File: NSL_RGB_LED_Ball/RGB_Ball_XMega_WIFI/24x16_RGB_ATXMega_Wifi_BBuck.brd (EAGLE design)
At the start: 46.4 x 123.7 mm, 118 parts, among them IC2 TLC5947XLP, IC3 TLC5947XLP, IC4 TLC5947XLP, IC5 MCP73123, IC6 CC3000, IC7 MMA7455L, IC8 OPA344, U1 TPS6120x, X1 NX3225GA-16.000M-STD-CRG-2

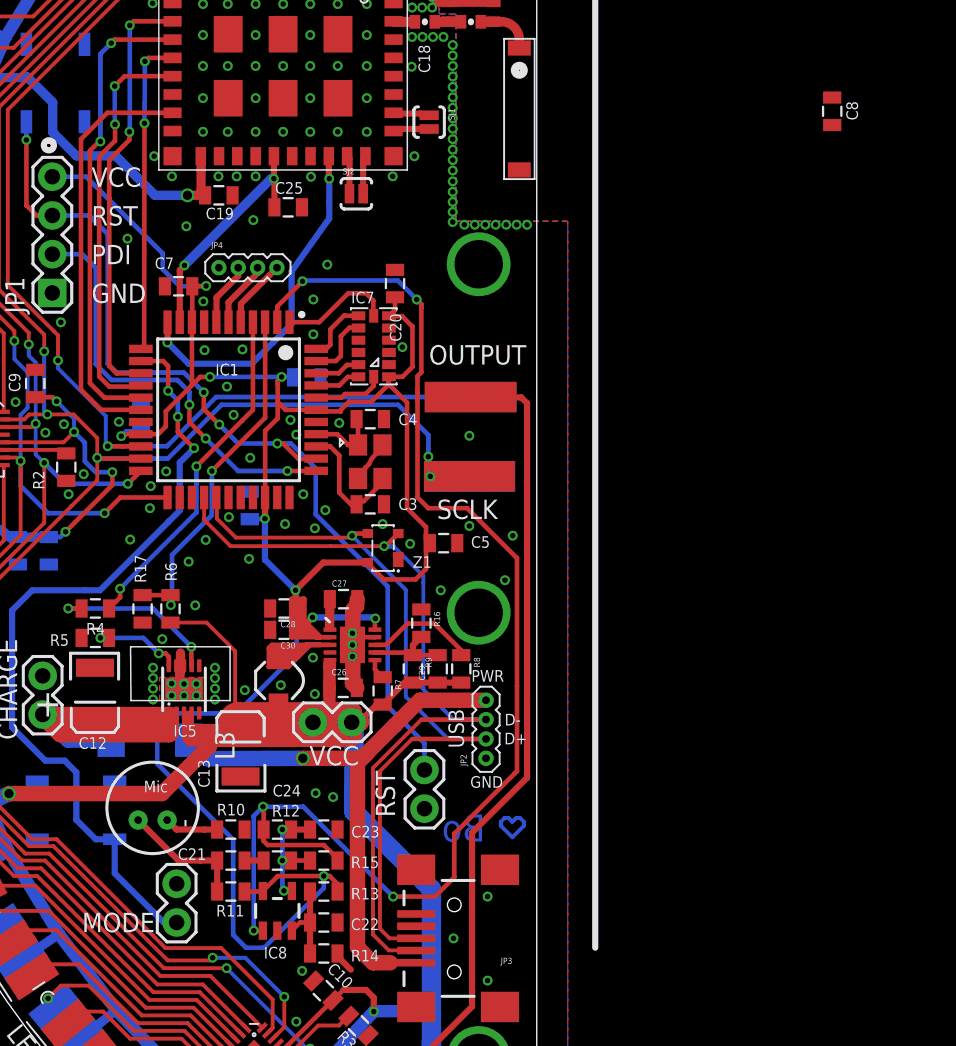
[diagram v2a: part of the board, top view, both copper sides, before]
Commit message: 
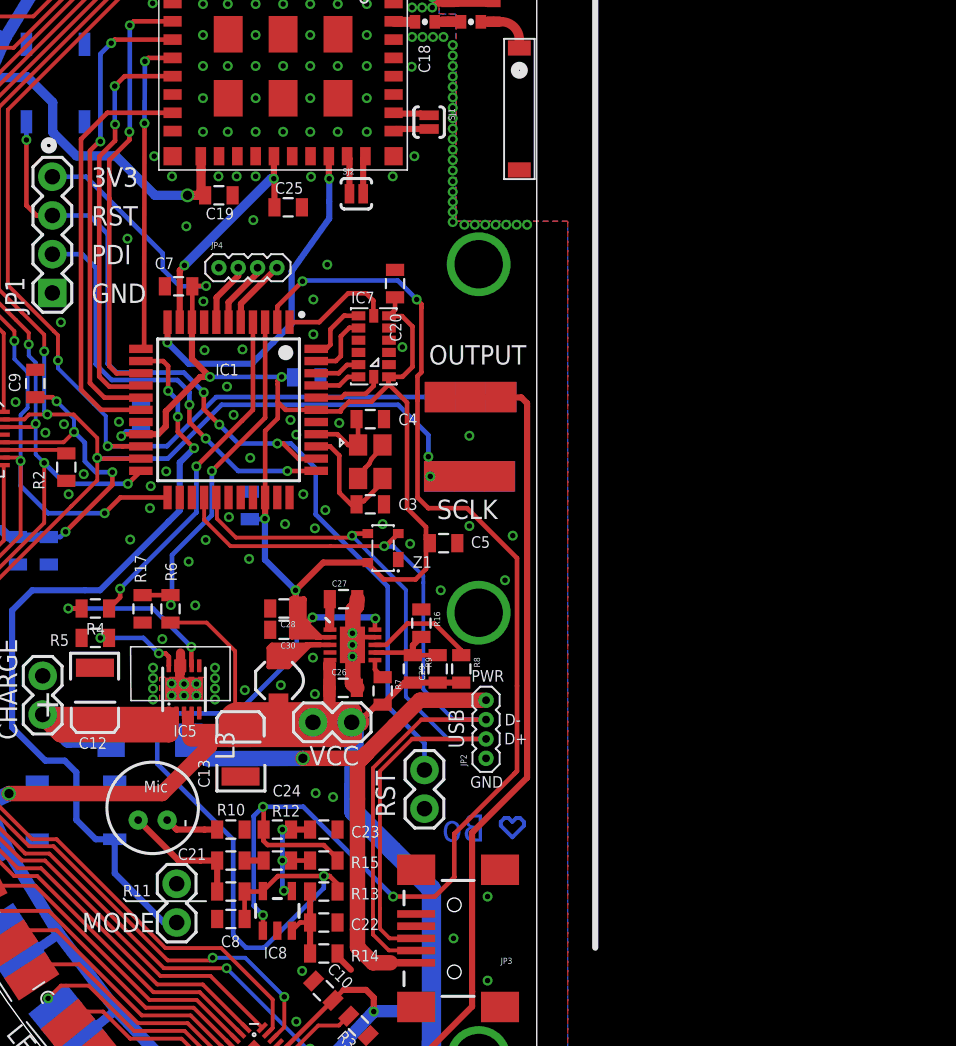
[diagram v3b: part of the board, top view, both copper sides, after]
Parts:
- moved C8 66.1 mm to (-37.8, -31.5), turned to 180 degrees
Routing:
- net +3V3: track 162.3 -> 164.1 mm
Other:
- board text added: "3V3"
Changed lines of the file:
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@@
 <text x="-46.99" y="11.43" size="1.27" layer="21" font="vector" ratio="12">PDI</text>
 <text x="-46.99" y="13.97" size="1.27" layer="21" font="vector" ratio="12">RST</text>
-<text x="-46.99" y="16.51" size="1.27" layer="21" font="vector" ratio="12">VCC</text>
+<text x="-46.99" y="16.51" size="1.27" layer="21" font="vector" ratio="12">3V3</text>
 <text x="-46.99" y="8.89" size="1.27" layer="21" font="vector" ratio="12">GND</text>
 <circle x="-49.784" y="19.2278" radius="0.331175" width="0.4064" layer="21"/>
@@
 <text x="-22.5806" y="-25.5524" size="1.778" layer="16" font="vector" ratio="12" rot="MR180" align="center">Bo</text>
 <wire x1="-13.9192" y1="32.3088" x2="11.6078" y2="32.3088" width="0" layer="21"/>
+<wire x1="-44.8818" y1="-30.1752" x2="-44.704" y2="-30.353" width="0.127" layer="21"/>
+<wire x1="-44.704" y1="-30.353" x2="-39.4716" y2="-30.353" width="0.127" layer="21"/>
 </plain>
 <attributes>
@@
 </element>
 <element name="R11" library="SparkFun" package="0805" value="2.2k" x="-37.846" y="-29.718" smashed="yes">
-<attribute name="NAME" x="-38.8112" y="-31.3563" size="0.762" layer="21" font="vector" ratio="12"/>
+<attribute name="NAME" x="-44.9326" y="-30.0355" size="0.762" layer="21" font="vector" ratio="12"/>
 <attribute name="VALUE" x="-38.862" y="-31.115" size="0.4064" layer="27"/>
 <attribute name="OC_NEWARK" value="61M5457" x="-37.846" y="-29.718" size="1.778" layer="27" display="off"/>
@@
 <attribute name="VALUE" x="-37.9984" y="1.8796" size="0.7" layer="21" ratio="5" rot="R270"/>
 </element>
-<element name="C8" library="SparkFun" package="0805" value="0.1uF" x="1.6002" y="21.463" smashed="yes" rot="R270">
-<attribute name="NAME" x="2.5273" y="22.1234" size="0.762" layer="21" font="vector" rot="R270"/>
-<attribute name="VALUE" x="0.2032" y="22.479" size="0.4064" layer="27" rot="R270"/>
+<element name="C8" library="SparkFun" package="0805" value="0.1uF" x="-37.846" y="-31.5214" smashed="yes" rot="R180">
+<attribute name="NAME" x="-37.2364" y="-32.6009" size="0.762" layer="21" font="vector" ratio="12" rot="R180"/>
+<attribute name="VALUE" x="-36.83" y="-30.1244" size="0.4064" layer="27" rot="R180"/>
 </element>
 <element name="X1" library="24x16_RGB_ATXMega_Wifi" package="NX3225GA" value="NX3225GA-16.000M-STD-CRG-2" x="-28.702" y="-1.524" smashed="yes" rot="R270"/>
@@
 <wire x1="-35.698" y1="-25.654" x2="-35.698" y2="-24.1952" width="0.3048" layer="1"/>
 <wire x1="-35.698" y1="-24.1952" x2="-35.7378" y2="-24.1554" width="0.3048" layer="1"/>
-<wire x1="-35.748" y1="-32.2881" x2="-36.3427" y2="-32.2881" width="0.3048" layer="1"/>
-<wire x1="-36.3427" y1="-32.2881" x2="-36.3474" y2="-32.2834" width="0.3048" layer="1"/>
-<via x="-36.3474" y="-32.2834" extent="1-16" drill="0.3556"/>
-<wire x1="-36.3474" y1="-32.2834" x2="-36.3474" y2="-24.765" width="0.3048" layer="16"/>
+<wire x1="-35.748" y1="-32.2881" x2="-35.7331" y2="-32.2881" width="0.3048" layer="1"/>
+<wire x1="-35.7331" y1="-32.2881" x2="-35.7378" y2="-31.2674" width="0.3048" layer="1"/>
+<via x="-35.7378" y="-31.2674" extent="1-16" drill="0.3556"/>
 <wire x1="-36.3474" y1="-24.765" x2="-35.7378" y2="-24.1554" width="0.3048" layer="16"/>
 <wire x1="-30.85" y1="-27.686" x2="-30.85" y2="-27.57" width="0.3048" layer="1"/>
@@
 <wire x1="-25.6032" y1="-3.8608" x2="-24.892" y2="-4.572" width="0.3048" layer="1"/>
 <wire x1="-24.892" y1="-4.572" x2="-22.352" y2="-4.572" width="0.3048" layer="1"/>
+<wire x1="-36.3474" y1="-24.765" x2="-36.3474" y2="-30.6578" width="0.3048" layer="16"/>
+<wire x1="-36.3474" y1="-30.6578" x2="-35.7378" y2="-31.2674" width="0.3048" layer="16"/>
 </signal>
 <signal name="CHARGE">
@@
 <via x="-32.3342" y="-16.764" extent="1-16" drill="0.3556"/>
 <via x="-34.5694" y="-16.1798" extent="1-16" drill="0.3556"/>
-<wire x1="-18.415" y1="14.0208" x2="1.6002" y2="20.563" width="0" layer="19" extent="1-1"/>
 </signal>
 <signal name="N$7">
@@
 <wire x1="-28.8638" y1="-8.1382" x2="-28.9306" y2="-8.205" width="0.3048" layer="1"/>
 <wire x1="-43.7484" y1="0.2796" x2="-43.7482" y2="0.2794" width="0.3048" layer="1"/>
-<wire x1="-43.7482" y1="0.2794" x2="-42.6212" y2="0.2794" width="0.3048" layer="1"/>
-<wire x1="-42.6212" y1="0.2794" x2="-42.1132" y2="0.7874" width="0.3048" layer="1"/>
-<wire x1="-42.1132" y1="0.7874" x2="-42.1132" y2="1.778" width="0.3048" layer="1"/>
-<wire x1="-42.1132" y1="1.778" x2="-40.3984" y2="3.4928" width="0.3048" layer="1"/>
-<wire x1="-40.3984" y1="3.4928" x2="-40.3984" y2="7.6296" width="0.3048" layer="1"/>
 <wire x1="-35.5984" y1="-3.8704" x2="-35.5984" y2="0.495" width="0.3048" layer="1"/>
-<wire x1="-40.3984" y1="3.4928" x2="-39.8526" y2="4.0386" width="0.3048" layer="1"/>
 <wire x1="-40.3984" y1="7.6296" x2="-40.375" y2="7.653" width="0.3048" layer="1"/>
 <wire x1="-40.375" y1="7.653" x2="-40.375" y2="9.9822" width="0.3048" layer="1"/>
@@
 <wire x1="-27.0764" y1="9.26" x2="-27.0764" y2="8.4422" width="0.3048" layer="1"/>
 <wire x1="-27.0764" y1="8.4422" x2="-27.4734" y2="8.0452" width="0.3048" layer="1"/>
-<wire x1="-39.8526" y1="4.0386" x2="-39.2176" y2="4.0386" width="0.3048" layer="1"/>
 <via x="-39.2176" y="4.0386" extent="1-16" drill="0.3556"/>
 <wire x1="-39.2176" y1="4.0386" x2="-34.5186" y2="4.0386" width="0.3048" layer="16"/>
@@
 <wire x1="-24.791421875" y1="-6.867346875" x2="-25.0444" y2="-6.61436875" width="0.3048" layer="1"/>
 <wire x1="-25.0444" y1="-6.61436875" x2="-25.0444" y2="-6.3246" width="0.3048" layer="1"/>
-<wire x1="-25.9334" y1="7.3406" x2="1.6002" y2="22.363" width="0" layer="19" extent="1-1"/>
+<wire x1="-40.3984" y1="7.6296" x2="-40.3984" y2="5.2194" width="0.4064" layer="1"/>
+<wire x1="-40.3984" y1="5.2194" x2="-39.2176" y2="4.0386" width="0.4064" layer="1"/>
+<wire x1="-43.7482" y1="0.2794" x2="-42.6212" y2="0.2794" width="0.4064" layer="1"/>
+<wire x1="-42.6212" y1="0.2794" x2="-42.1132" y2="0.7874" width="0.4064" layer="1"/>
+<wire x1="-42.1132" y1="0.7874" x2="-42.1132" y2="1.778" width="0.4064" layer="1"/>
+<wire x1="-42.1132" y1="1.778" x2="-39.8526" y2="4.0386" width="0.4064" layer="1"/>
+<wire x1="-39.8526" y1="4.0386" x2="-39.2176" y2="4.0386" width="0.4064" layer="1"/>
+<wire x1="-36.946" y1="-31.5214" x2="-36.946" y2="-29.718" width="0.3048" layer="1"/>
 </signal>
 <signal name="N$24">

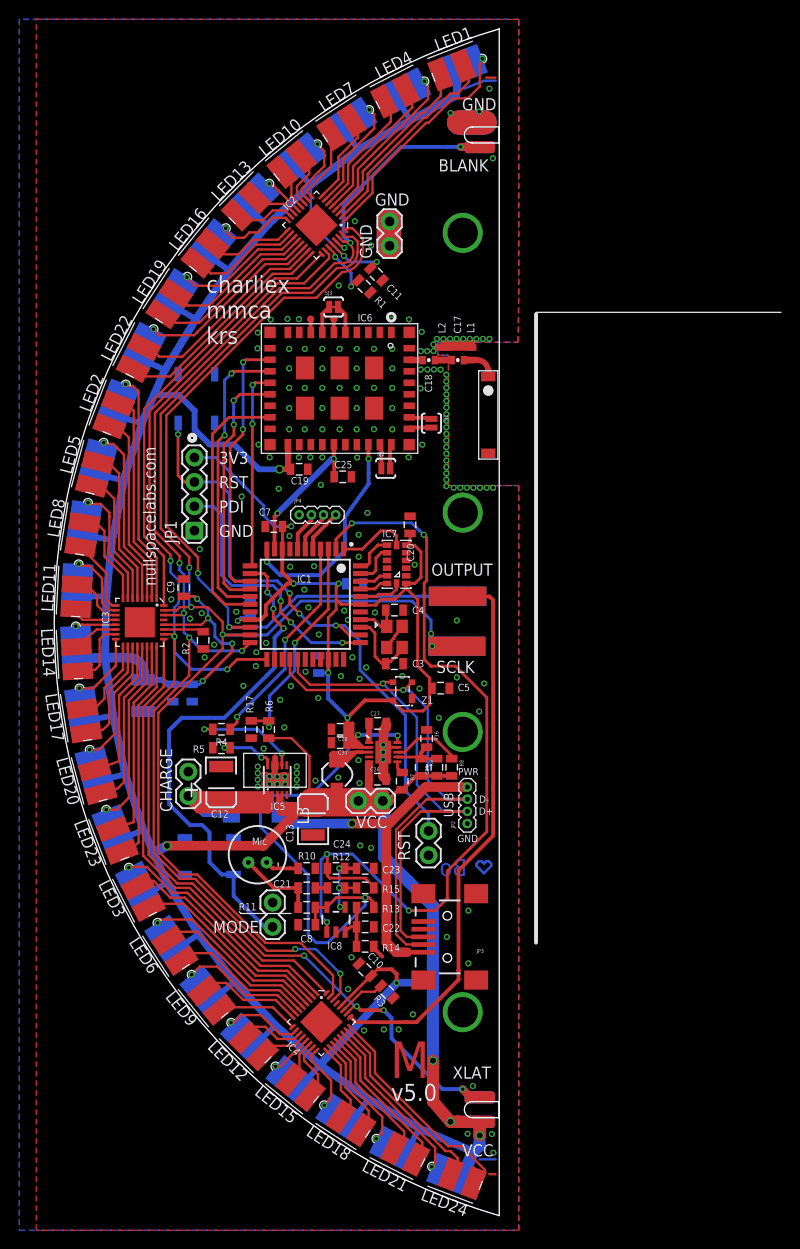
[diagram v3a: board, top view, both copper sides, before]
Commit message: 
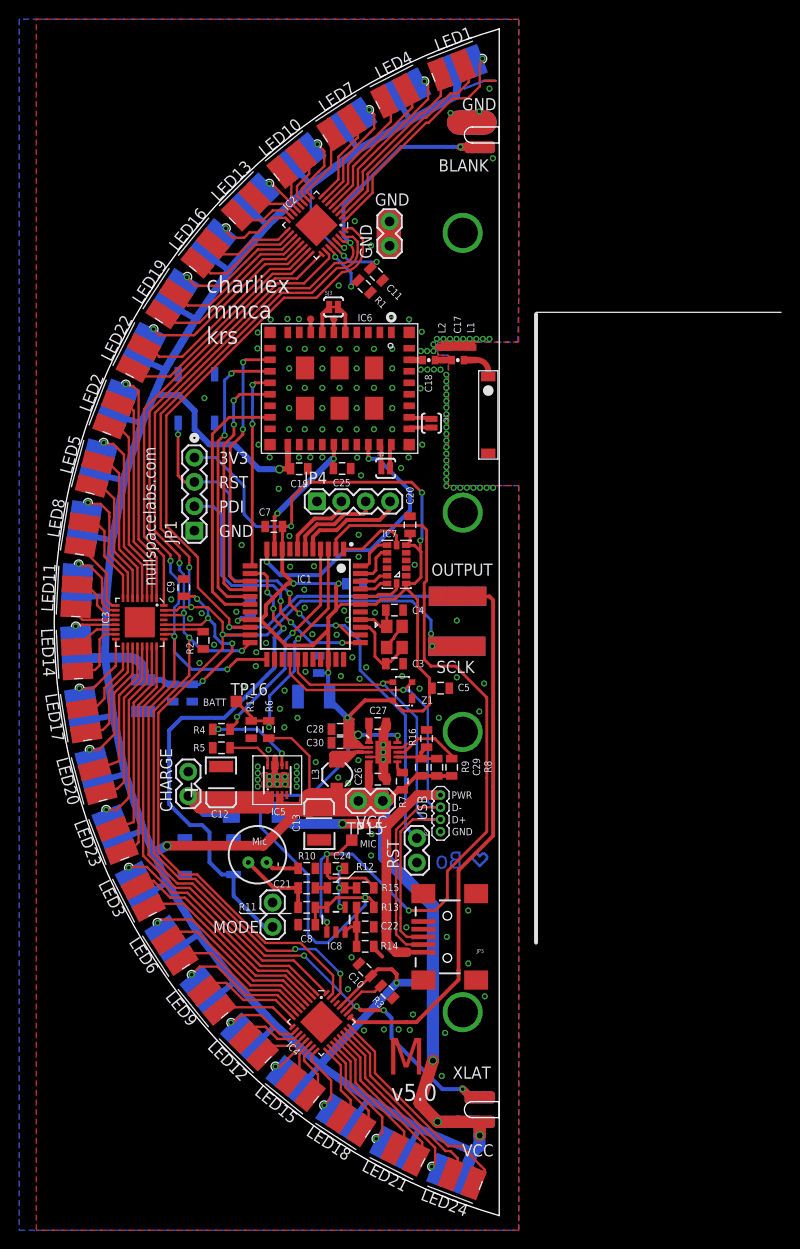
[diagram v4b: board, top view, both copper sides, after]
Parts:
- added C31: 12pF, SparkFun:0805
- added C32: 1uF, 24x16_RGB:0805
- added TP15: MIC, testpad:TP12SQ
- added TP16: BATT, testpad:TP12SQ
- C23: value .1uF -> 47uF; device SparkFun:0805 -> slice_noshift:EIA3528
- JP4: device SparkFun-Connectors:1X04-1.27MM -> SparkFun-Connectors:1X04
- R1, R2, R3: value 47K -> 20K
- moved C23 18.7 mm to (-37.1, -7.75), flipped to the bottom, turned to 180 degrees
- moved JP2 2.92 mm to (-23.9, -21.8)
- moved JP4 2.32 mm to (-36.8, 12.6)
- moved RST 1.44 mm to (-26.4, -25.0)
- moved C25 0.87 mm to (-34.2, 16.0)
- moved C13 0.83 mm to (-36.6, -21.0)
- moved C19 0.05 mm to (-38.6, 16.0)
- moved C26 0.05 mm to (-30.4, -16.4)
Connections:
- net +3V3: now also C23.A, C31.1, C32.1
- net BATTSENSE: now also TP16.TP
- net GND: now also C23.C, C31.2, C32.2; no longer C23.2
- net MIC: now also TP15.TP
- net N$17: no longer C23.1
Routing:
- net +3V3: track 164.1 -> 203.7 mm, vias 9 -> 11
- net UP: track 4.56 -> 11.3 mm
- net VCC: track 453.5 -> 459.9 mm
- net VBAT_SW_EN: track 23.2 -> 28.9 mm
- net GND: track 38.7 -> 44.2 mm, vias 177 -> 179
- net SELECT: track 4.36 -> 9.78 mm
- net D-: track 53.9 -> 49.7 mm
- net D+: track 51.2 -> 47.3 mm
- net DOWN: track 4.17 -> 7.90 mm
- net MIC: track 87.9 -> 91.3 mm, vias 5 -> 3
- net N$7: track 38.8 -> 35.7 mm
- net BATTSENSE: track 23.6 -> 26.3 mm
- net N$1: track 11.3 -> 9.54 mm
- net N$34: track 1.68 -> 0.00 mm
- net N$17: track 8.22 -> 6.97 mm
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
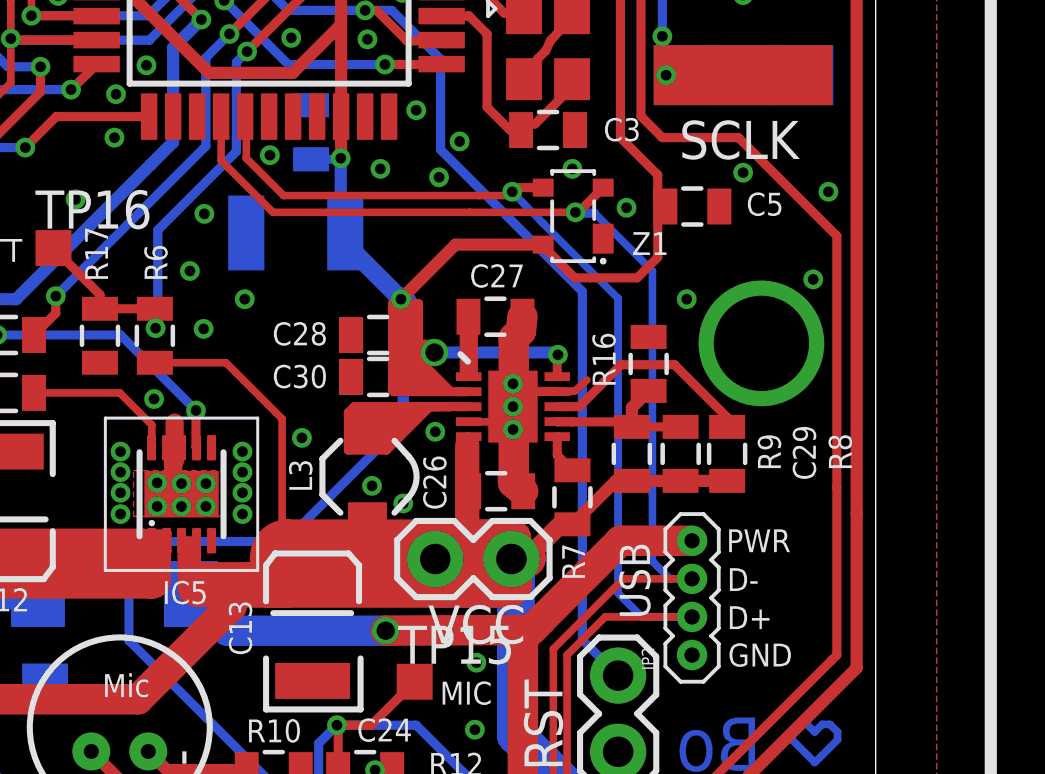
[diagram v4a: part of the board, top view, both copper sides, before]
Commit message: Changed to Buck Boost
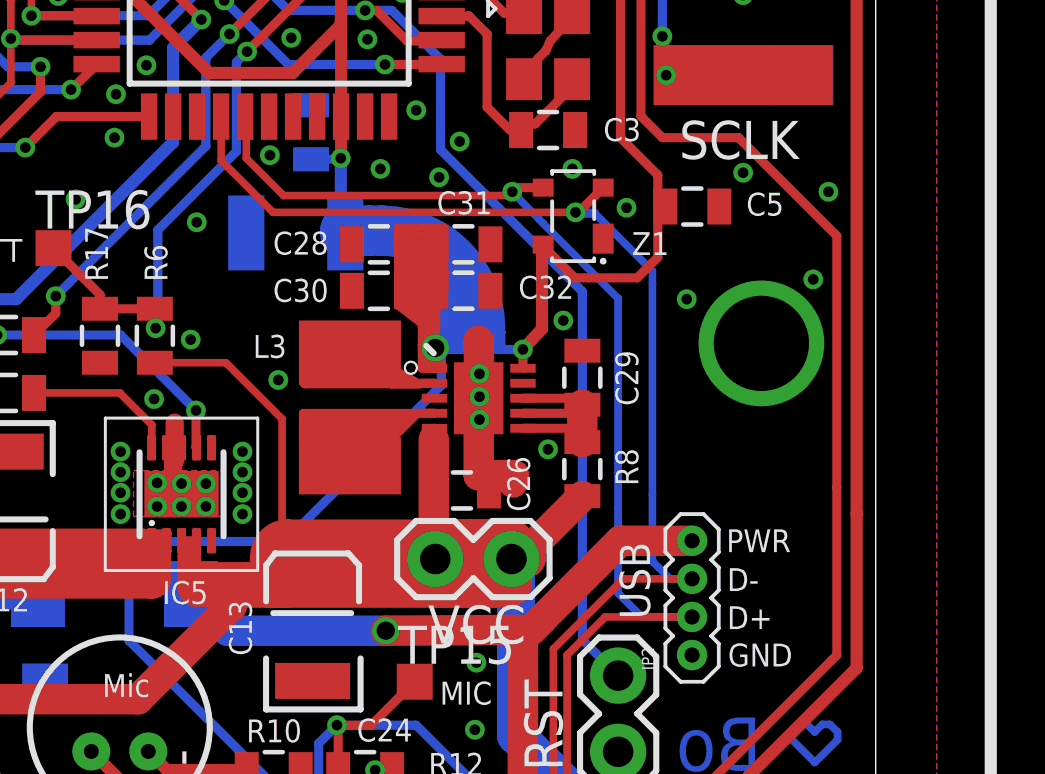
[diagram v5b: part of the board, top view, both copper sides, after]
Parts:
- removed C27: 0.1, CH_passive:0805
- removed R16, R9: see notes, CH_passive:0805
- removed R7: 1M, CH_passive:0805
- removed U1: TPS6120x, CH_TI:QFN_10_PAD
- added IC9: TPS6300X, 24x16_RGB_ATXMega_Wifi_BBuck:QFN_10_PAD
- L3: value 2.2uH 1.6A -> (none); device CH_passive:1_3X1_3 -> rcl:L1812
- R8: value 1M -> 100R
- moved C31 5.26 mm to (-31.5, -8.13), flipped to the top
- moved R8 4.85 mm to (-27.6, -15.6)
- moved C29 4.15 mm to (-27.6, -12.6), turned to 270 degrees
- moved C32 3.20 mm to (-31.5, -9.68), flipped to the top
- moved C28 3.02 mm to (-34.3, -8.13)
- moved C30 2.87 mm to (-34.3, -9.68)
- moved L3 2.38 mm to (-35.3, -13.6)
- moved C26 1.14 mm to (-31.6, -16.3)
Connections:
- removed net EN: R7.1, U1.6
- removed net PS: R8.1, U1.8
- removed net UVLO: C29.2, R16.2, R9.1, U1.7
- new net N$32: C29.2, IC9.6, IC9.7, IC9.8, R8.1
- net +3V3: now also IC9.1, IC9.10; no longer U1.10, U1.2
- net GND: now also C29.1, IC9.3, IC9.9, IC9.PAD@1, IC9.PAD@2, IC9.PAD@3, IC9.PAD@4, IC9.PAD@5; no longer C27.2, R16.1, U1.4, U1.9, U1.PAD@1, U1.PAD@2, U1.PAD@3, U1.PAD@4, U1.PAD@5
- net N$24: now also IC9.2, L3.2; no longer L3.P$2, U1.3
- net N$30: now also IC9.4, L3.1; no longer C27.1, U1.1
- net VCC: now also IC9.5; no longer C29.1, L3.P$1, R7.2, R9.2, U1.5
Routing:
- net +3V3: track 203.7 -> 225.7 mm, vias 11 -> 10
- net N$30: track 2.79 -> 24.6 mm
- net GND: track 44.2 -> 36.0 mm, vias 179 -> 176
- net N$32: track 0.00 -> 7.58 mm
- net PS: track 7.49 -> 0.00 mm
- net UVLO: track 6.36 -> 0.00 mm
- net VCC: track 459.9 -> 454.3 mm
- net N$24: track 16.9 -> 18.7 mm
- net EN: track 1.33 -> 0.00 mm
